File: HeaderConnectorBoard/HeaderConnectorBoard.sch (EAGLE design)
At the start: 2 parts

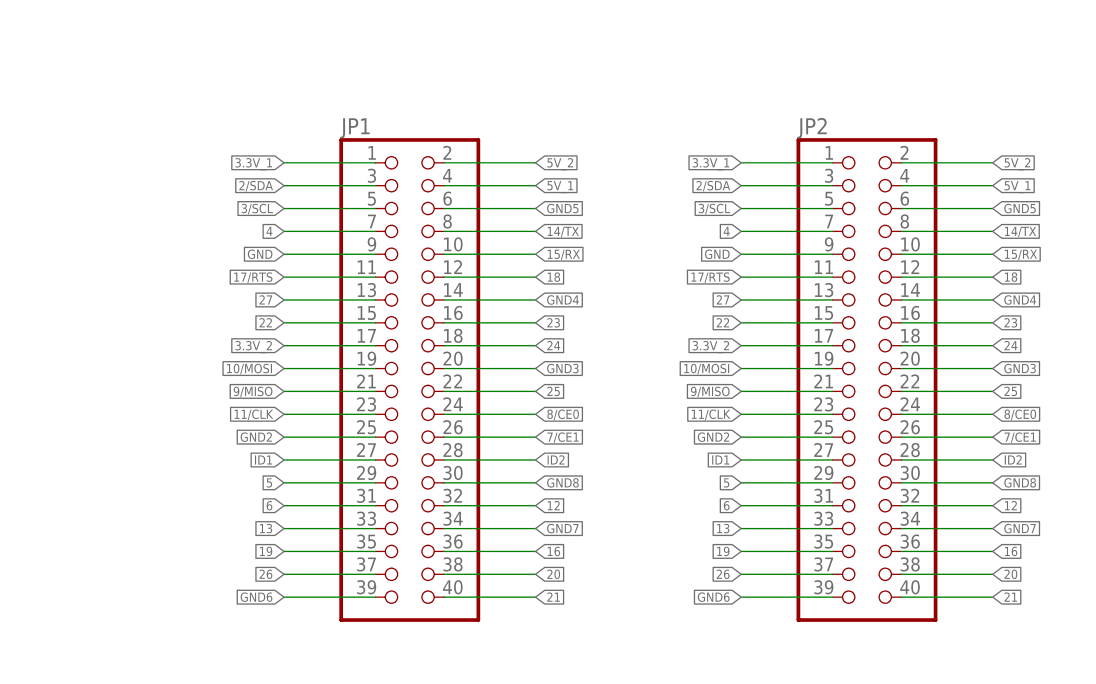
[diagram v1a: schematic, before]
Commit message: Lid conn - added POWER LED
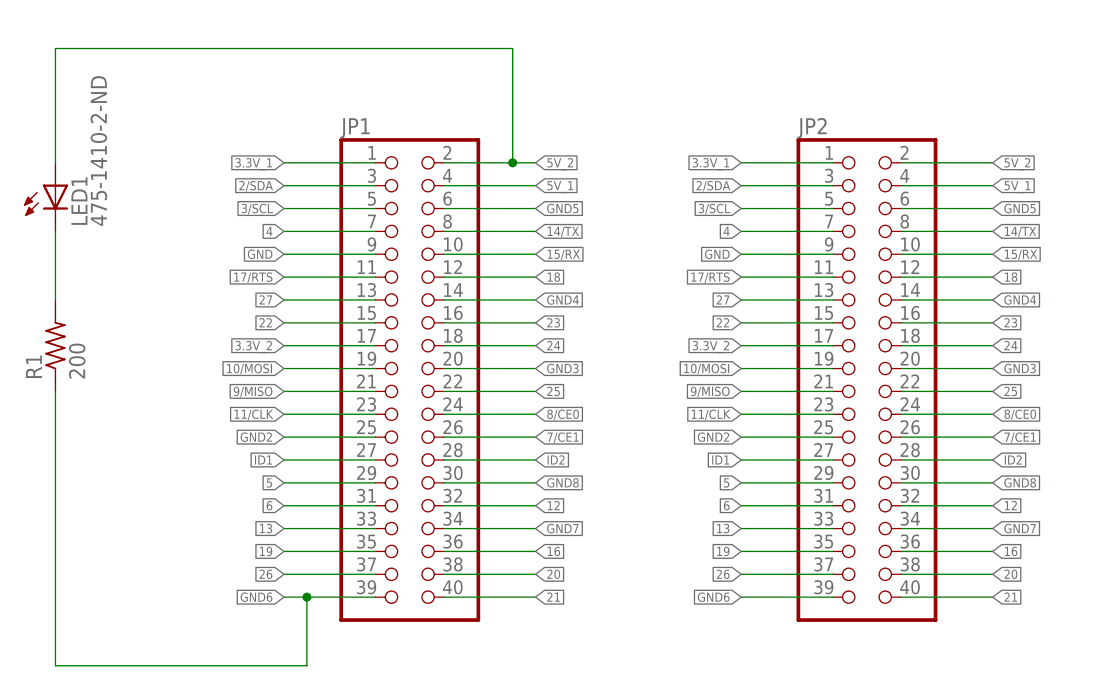
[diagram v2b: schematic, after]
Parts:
- added LED1: 475-1410-2-ND, led:LEDCHIPLED_0805
- added R1: 200, resistor:R-US_R0805
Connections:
- new net N$1: LED1.C, R1.2
- net 5V_2: now also LED1.A
- net GND6: now also R1.1
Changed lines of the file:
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@@
 <?xml version="1.0" encoding="utf-8"?>
 <!DOCTYPE eagle SYSTEM "eagle.dtd">
-<eagle version="7.1.0">
+<eagle version="7.6.0">
 <drawing>
 <settings>
@@
 <setting verticaltext="up"/>
 </settings>
-<grid distance="0.1" unitdist="inch" unit="inch" style="lines" multiple="1" display="yes" altdistance="0.01" altunitdist="inch" altunit="inch"/>
+<grid distance="0.1" unitdist="inch" unit="inch" style="lines" multiple="1" display="no" altdistance="0.01" altunitdist="inch" altunit="inch"/>
 <layers>
 <layer number="1" name="Top" color="4" fill="1" visible="no" active="no"/>
 <layer number="2" name="Route2" color="1" fill="3" visible="no" active="no"/>
 <layer number="3" name="Route3" color="4" fill="3" visible="no" active="no"/>
+<layer number="4" name="Route4" color="1" fill="4" visible="no" active="no"/>
+<layer number="5" name="Route5" color="4" fill="4" visible="no" active="no"/>
+<layer number="6" name="Route6" color="1" fill="8" visible="no" active="no"/>
+<layer number="7" name="Route7" color="4" fill="8" visible="no" active="no"/>
+<layer number="8" name="Route8" color="1" fill="2" visible="no" active="no"/>
+<layer number="9" name="Route9" color="4" fill="2" visible="no" active="no"/>
+<layer number="10" name="Route10" color="1" fill="7" visible="no" active="no"/>
+<layer number="11" name="Route11" color="4" fill="7" visible="no" active="no"/>
+<layer number="12" name="Route12" color="1" fill="5" visible="no" active="no"/>
+<layer number="13" name="Route13" color="4" fill="5" visible="no" active="no"/>
 <layer number="14" name="Route14" color="1" fill="6" visible="no" active="no"/>
 <layer number="15" name="Route15" color="4" fill="6" visible="no" active="no"/>
@@
 <layer number="97" name="Info" color="7" fill="1" visible="yes" active="yes"/>
 <layer number="98" name="Guide" color="6" fill="1" visible="yes" active="yes"/>
+<layer number="99" name="SpiceOrder" color="5" fill="1" visible="yes" active="yes"/>
 </layers>
 <schematic xreflabel="%F%N/%S.%C%R" xrefpart="/%S.%C%R">
@@
 <part name="JP2" library="HeaderConnectorBoard" deviceset="PINHD-2X20" device=""/>
 <part name="FRAME1" library="frames" deviceset="LETTER_L" device=""/>
+<part name="LED1" library="led" deviceset="LED" device="CHIPLED_0805" value="475-1410-2-ND"/>
+<part name="R1" library="resistor" deviceset="R-US_" device="R0805" value="200"/>
 </parts>
 <sheets>
@@
 <instance part="FRAME1" gate="G$1" x="-68.58" y="-12.7"/>
 <instance part="FRAME1" gate="G$2" x="78.74" y="-12.7"/>
+<instance part="LED1" gate="G$1" x="-2.54" y="101.6"/>
+<instance part="R1" gate="G$1" x="-2.54" y="83.82" rot="R90"/>
 </instances>
 <busses>
@@
 <segment>
 <label x="50.8" y="104.14" size="1.016" layer="95" xref="yes"/>
-<wire x1="50.8" y1="104.14" x2="40.64" y2="104.14" width="0.1524" layer="91"/>
+<wire x1="50.8" y1="104.14" x2="48.26" y2="104.14" width="0.1524" layer="91"/>
 <pinref part="JP1" gate="A" pin="2"/>
+<pinref part="LED1" gate="G$1" pin="A"/>
+<wire x1="48.26" y1="104.14" x2="40.64" y2="104.14" width="0.1524" layer="91"/>
+<wire x1="-2.54" y1="104.14" x2="-2.54" y2="116.84" width="0.1524" layer="91"/>
+<wire x1="-2.54" y1="116.84" x2="48.26" y2="116.84" width="0.1524" layer="91"/>
+<wire x1="48.26" y1="116.84" x2="48.26" y2="104.14" width="0.1524" layer="91"/>
+<junction x="48.26" y="104.14"/>
 </segment>
 <segment>
@@
 <segment>
 <pinref part="JP1" gate="A" pin="39"/>
-<wire x1="33.02" y1="55.88" x2="22.86" y2="55.88" width="0.1524" layer="91"/>
+<wire x1="33.02" y1="55.88" x2="25.4" y2="55.88" width="0.1524" layer="91"/>
 <label x="22.86" y="55.88" size="1.016" layer="95" rot="R180" xref="yes"/>
+<pinref part="R1" gate="G$1" pin="1"/>
+<wire x1="25.4" y1="55.88" x2="22.86" y2="55.88" width="0.1524" layer="91"/>
+<wire x1="-2.54" y1="78.74" x2="-2.54" y2="48.26" width="0.1524" layer="91"/>
+<wire x1="-2.54" y1="48.26" x2="25.4" y2="48.26" width="0.1524" layer="91"/>
+<wire x1="25.4" y1="48.26" x2="25.4" y2="55.88" width="0.1524" layer="91"/>
+<junction x="25.4" y="55.88"/>
 </segment>
 <segment>
@@
 </segment>
 </net>
+<net name="N$1" class="0">
+<segment>
+<pinref part="LED1" gate="G$1" pin="C"/>
+<pinref part="R1" gate="G$1" pin="2"/>
+<wire x1="-2.54" y1="96.52" x2="-2.54" y2="88.9" width="0.1524" layer="91"/>
+</segment>
+</net>

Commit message: lid conn - labels were flipped (and thus power led broken)
JP1/JP2 had all labelled flipped, which previously was a don't care because the connectors were
connected straight thru, and no labels were used.  When power was added, it was to the wrong pins
because the labels were wrong.  Both are now fixed.
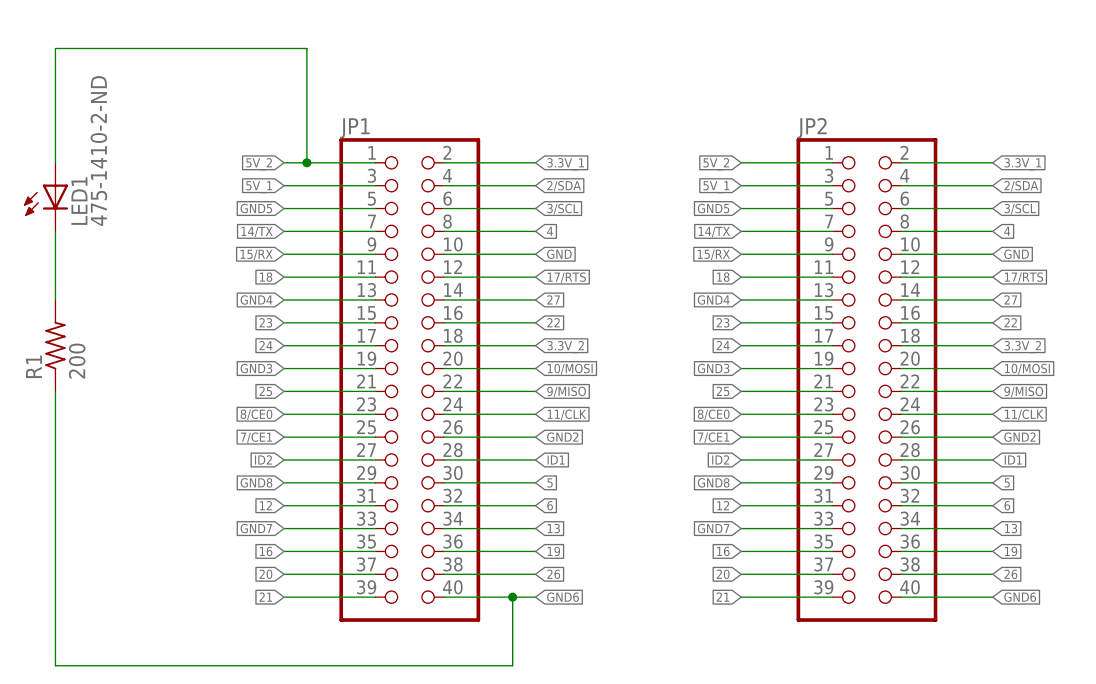
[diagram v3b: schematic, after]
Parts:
- JP1, JP2: value (none) -> NONE
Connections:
- net 10/MOSI: now also JP1.20, JP2.20; no longer JP1.19, JP2.19
- net 11/CLK: now also JP1.24, JP2.24; no longer JP1.23, JP2.23
- net 12: now also JP1.31, JP2.31; no longer JP1.32, JP2.32
- net 13: now also JP1.34, JP2.34; no longer JP1.33, JP2.33
- net 14/TX: now also JP1.7, JP2.7; no longer JP1.8, JP2.8
- net 15/RX: now also JP1.9, JP2.9; no longer JP1.10, JP2.10
- net 16: now also JP1.35, JP2.35; no longer JP1.36, JP2.36
- net 17/RTS: now also JP1.12, JP2.12; no longer JP1.11, JP2.11
- net 18: now also JP1.11, JP2.11; no longer JP1.12, JP2.12
- net 19: now also JP1.36, JP2.36; no longer JP1.35, JP2.35
- net 2/SDA: now also JP1.4, JP2.4; no longer JP1.3, JP2.3
- net 20: now also JP1.37, JP2.37; no longer JP1.38, JP2.38
- net 21: now also JP1.39, JP2.39; no longer JP1.40, JP2.40
- net 22: now also JP1.16, JP2.16; no longer JP1.15, JP2.15
- net 23: now also JP1.15, JP2.15; no longer JP1.16, JP2.16
- net 24: now also JP1.17, JP2.17; no longer JP1.18, JP2.18
- net 25: now also JP1.21, JP2.21; no longer JP1.22, JP2.22
- net 26: now also JP1.38, JP2.38; no longer JP1.37, JP2.37
- net 27: now also JP1.14, JP2.14; no longer JP1.13, JP2.13
- net 3.3V_1: now also JP1.2, JP2.2; no longer JP1.1, JP2.1
- net 3.3V_2: now also JP1.18, JP2.18; no longer JP1.17, JP2.17
- net 3/SCL: now also JP1.6, JP2.6; no longer JP1.5, JP2.5
- net 4: now also JP1.8, JP2.8; no longer JP1.7, JP2.7
- net 5: now also JP1.30, JP2.30; no longer JP1.29, JP2.29
- net 5V_1: now also JP1.3, JP2.3; no longer JP1.4, JP2.4
- net 5V_2: now also JP1.1, JP2.1; no longer JP1.2, JP2.2
- net 6: now also JP1.32, JP2.32; no longer JP1.31, JP2.31
- net 7/CE1: now also JP1.25, JP2.25; no longer JP1.26, JP2.26
- net 8/CE0: now also JP1.23, JP2.23; no longer JP1.24, JP2.24
- net 9/MISO: now also JP1.22, JP2.22; no longer JP1.21, JP2.21
- net GND: now also JP1.10, JP2.10; no longer JP1.9, JP2.9
- net GND2: now also JP1.26, JP2.26; no longer JP1.25, JP2.25
- net GND3: now also JP1.19, JP2.19; no longer JP1.20, JP2.20
- net GND4: now also JP1.13, JP2.13; no longer JP1.14, JP2.14
- net GND5: now also JP1.5, JP2.5; no longer JP1.6, JP2.6
- net GND6: now also JP1.40, JP2.40; no longer JP1.39, JP2.39
- net GND7: now also JP1.33, JP2.33; no longer JP1.34, JP2.34
- net GND8: now also JP1.29, JP2.29; no longer JP1.30, JP2.30
- net ID1: now also JP1.28, JP2.28; no longer JP1.27, JP2.27
- net ID2: now also JP1.27, JP2.27; no longer JP1.28, JP2.28
